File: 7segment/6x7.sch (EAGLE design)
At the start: 22 parts, among them IC1 AT90S2313P, IC2 7805TV

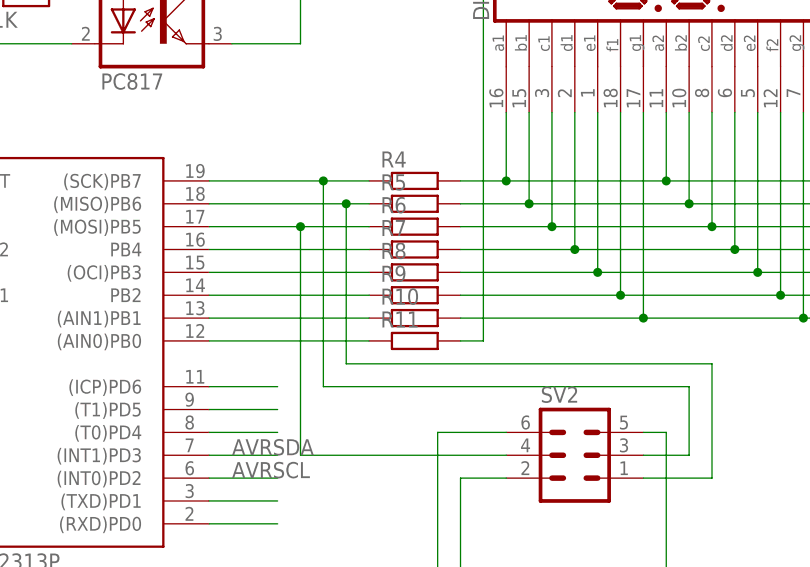
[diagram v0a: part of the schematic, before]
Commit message: 7segment 6x7: Add LED resistor values
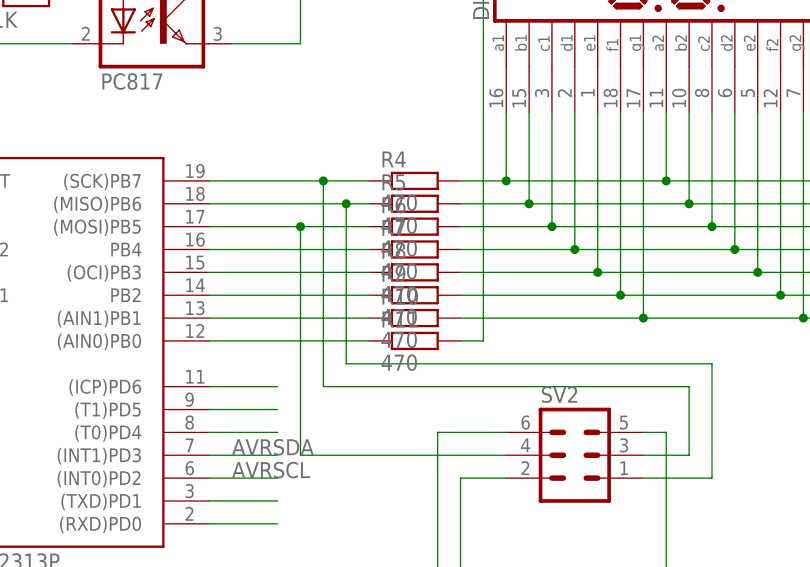
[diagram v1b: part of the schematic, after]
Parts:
- R10, R11, R4, R5, R6, R7, R8, R9: value (none) -> 470
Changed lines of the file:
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@@
 <part name="DIS2" library="display-hp" deviceset="HD-K121" device=""/>
 <part name="DIS3" library="display-hp" deviceset="HD-K121" device=""/>
-<part name="R4" library="rcl" deviceset="R-EU_" device="0207/10"/>
-<part name="R5" library="rcl" deviceset="R-EU_" device="0207/10"/>
-<part name="R6" library="rcl" deviceset="R-EU_" device="0207/10"/>
-<part name="R7" library="rcl" deviceset="R-EU_" device="0207/10"/>
-<part name="R8" library="rcl" deviceset="R-EU_" device="0207/10"/>
-<part name="R9" library="rcl" deviceset="R-EU_" device="0207/10"/>
-<part name="R10" library="rcl" deviceset="R-EU_" device="0207/10"/>
-<part name="R11" library="rcl" deviceset="R-EU_" device="0207/10"/>
+<part name="R4" library="rcl" deviceset="R-EU_" device="0207/10" value="470"/>
+<part name="R5" library="rcl" deviceset="R-EU_" device="0207/10" value="470"/>
+<part name="R6" library="rcl" deviceset="R-EU_" device="0207/10" value="470"/>
+<part name="R7" library="rcl" deviceset="R-EU_" device="0207/10" value="470"/>
+<part name="R8" library="rcl" deviceset="R-EU_" device="0207/10" value="470"/>
+<part name="R9" library="rcl" deviceset="R-EU_" device="0207/10" value="470"/>
+<part name="R10" library="rcl" deviceset="R-EU_" device="0207/10" value="470"/>
+<part name="R11" library="rcl" deviceset="R-EU_" device="0207/10" value="470"/>
 <part name="SV2" library="con-harting-ml" deviceset="ML6" device=""/>
 </parts>

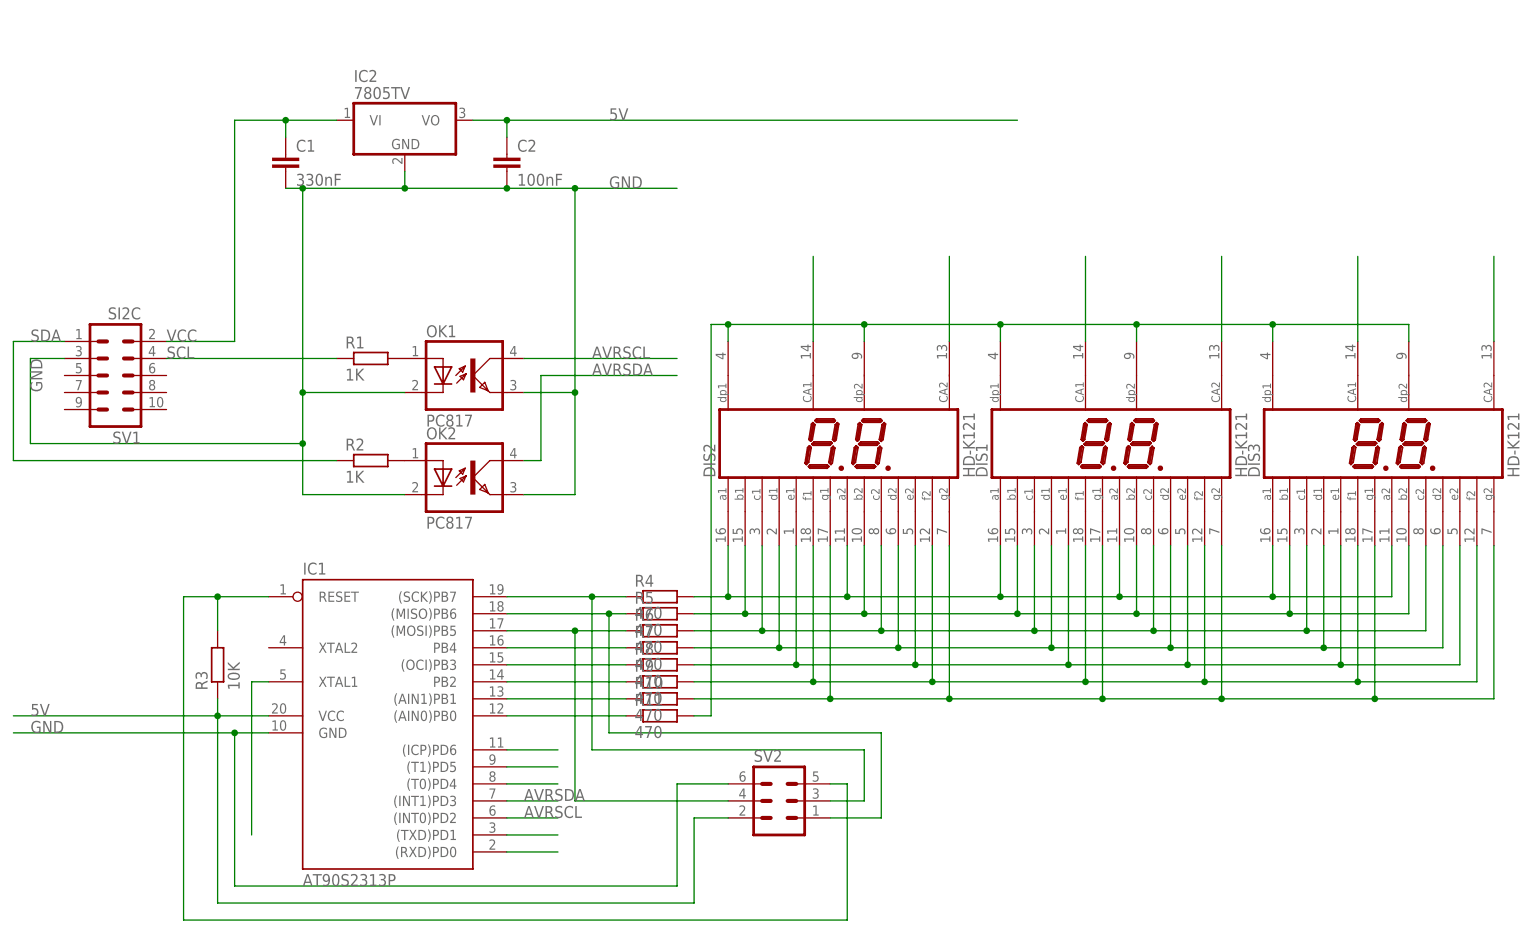
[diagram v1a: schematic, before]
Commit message: 7segment: schematic: add drill holes and netname labels
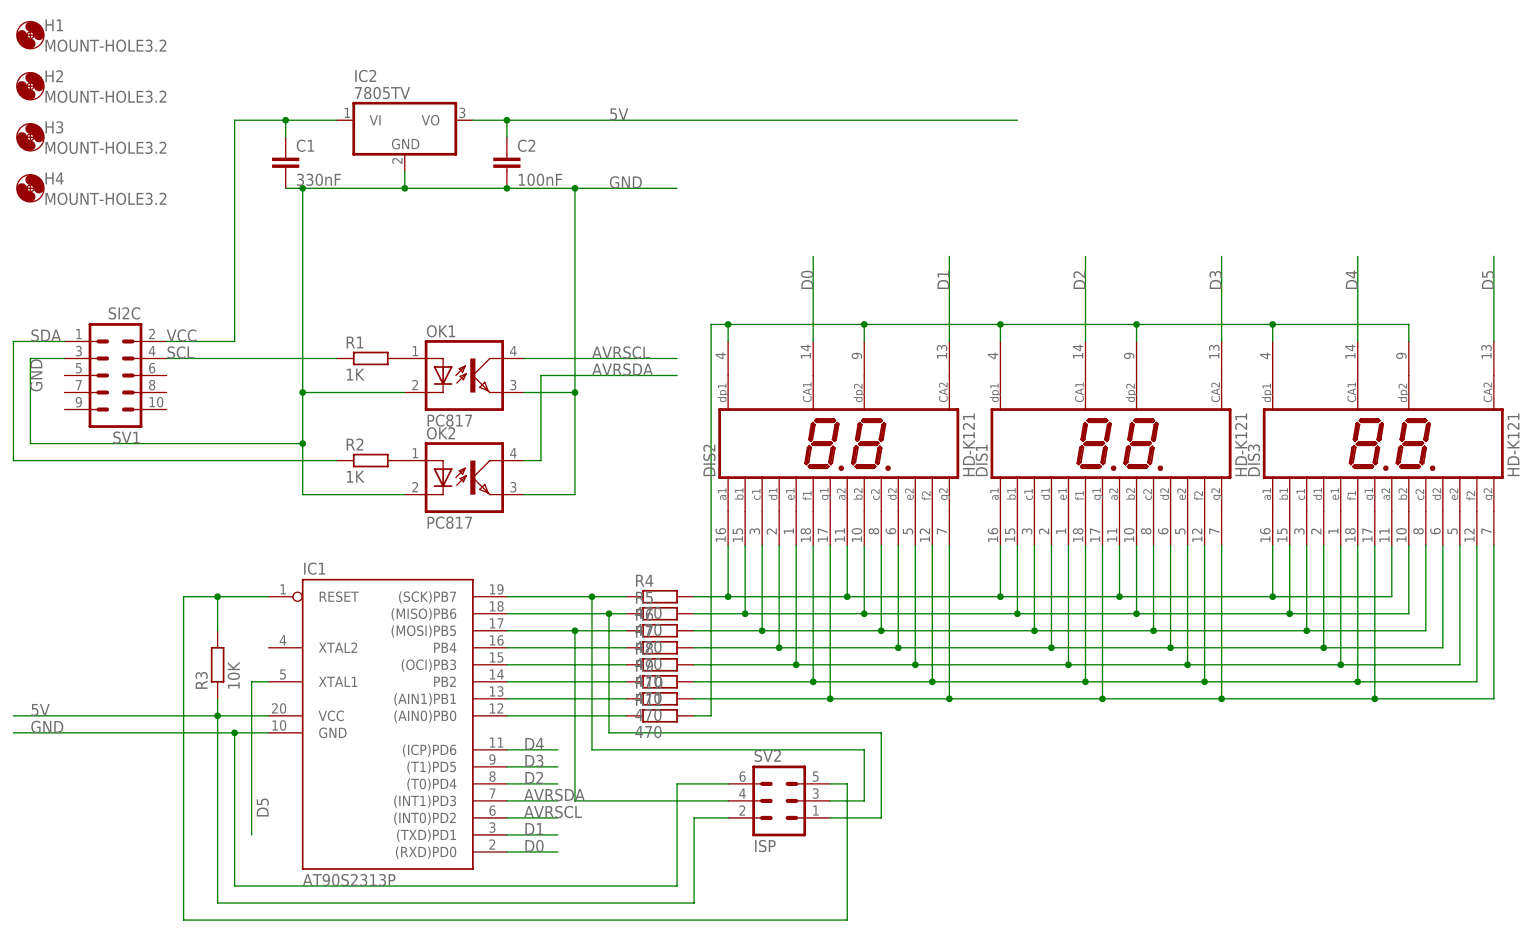
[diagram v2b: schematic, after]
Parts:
- added H1, H2, H3, H4: MOUNT-HOLE3.2, holes:MOUNT-HOLE3.2
- SV2: value (none) -> ISP
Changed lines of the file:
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@@
 <part name="R10" library="rcl" deviceset="R-EU_" device="0207/10" value="470"/>
 <part name="R11" library="rcl" deviceset="R-EU_" device="0207/10" value="470"/>
-<part name="SV2" library="con-harting-ml" deviceset="ML6" device=""/>
+<part name="SV2" library="con-harting-ml" deviceset="ML6" device="" value="ISP"/>
+<part name="H1" library="holes" deviceset="MOUNT-HOLE" device="3.2"/>
+<part name="H2" library="holes" deviceset="MOUNT-HOLE" device="3.2"/>
+<part name="H3" library="holes" deviceset="MOUNT-HOLE" device="3.2"/>
+<part name="H4" library="holes" deviceset="MOUNT-HOLE" device="3.2"/>
 </parts>
 <sheets>
@@
 <instance part="R11" gate="G$1" x="27.94" y="0"/>
 <instance part="SV2" gate="1" x="45.72" y="-12.7"/>
+<instance part="H1" gate="G$1" x="-66.04" y="101.6"/>
+<instance part="H2" gate="G$1" x="-66.04" y="93.98"/>
+<instance part="H3" gate="G$1" x="-66.04" y="86.36"/>
+<instance part="H4" gate="G$1" x="-66.04" y="78.74"/>
 </instances>
 <busses>
@@
 <pinref part="IC1" gate="G$1" pin="(RXD)PD0"/>
 <wire x1="5.08" y1="-20.32" x2="12.7" y2="-20.32" width="0.1524" layer="91"/>
+<label x="7.62" y="-20.32" size="1.778" layer="95"/>
 </segment>
 <segment>
 <pinref part="DIS2" gate="R" pin="CA1"/>
 <wire x1="50.8" y1="55.88" x2="50.8" y2="68.58" width="0.1524" layer="91"/>
+<label x="50.8" y="63.5" size="1.778" layer="95" rot="R90"/>
 </segment>
 </net>
@@
 <pinref part="IC1" gate="G$1" pin="(TXD)PD1"/>
 <wire x1="5.08" y1="-17.78" x2="12.7" y2="-17.78" width="0.1524" layer="91"/>
+<label x="7.62" y="-17.78" size="1.778" layer="95"/>
 </segment>
 <segment>
 <pinref part="DIS2" gate="R" pin="CA2"/>
 <wire x1="71.12" y1="55.88" x2="71.12" y2="68.58" width="0.1524" layer="91"/>
+<label x="71.12" y="63.5" size="1.778" layer="95" rot="R90"/>
 </segment>
 </net>
@@
 <pinref part="IC1" gate="G$1" pin="(T0)PD4"/>
 <wire x1="5.08" y1="-10.16" x2="12.7" y2="-10.16" width="0.1524" layer="91"/>
+<label x="7.62" y="-10.16" size="1.778" layer="95"/>
 </segment>
 <segment>
 <pinref part="DIS1" gate="R" pin="CA1"/>
 <wire x1="91.44" y1="55.88" x2="91.44" y2="68.58" width="0.1524" layer="91"/>
+<label x="91.44" y="63.5" size="1.778" layer="95" rot="R90"/>
 </segment>
 </net>
@@
 <pinref part="IC1" gate="G$1" pin="(T1)PD5"/>
 <wire x1="5.08" y1="-7.62" x2="12.7" y2="-7.62" width="0.1524" layer="91"/>
+<label x="7.62" y="-7.62" size="1.778" layer="95"/>
 </segment>
 <segment>
 <pinref part="DIS1" gate="R" pin="CA2"/>
 <wire x1="111.76" y1="55.88" x2="111.76" y2="68.58" width="0.1524" layer="91"/>
+<label x="111.76" y="63.5" size="1.778" layer="95" rot="R90"/>
 </segment>
 </net>
@@
 <pinref part="IC1" gate="G$1" pin="(ICP)PD6"/>
 <wire x1="5.08" y1="-5.08" x2="12.7" y2="-5.08" width="0.1524" layer="91"/>
+<label x="7.62" y="-5.08" size="1.778" layer="95"/>
 </segment>
 <segment>
 <pinref part="DIS3" gate="R" pin="CA1"/>
 <wire x1="132.08" y1="55.88" x2="132.08" y2="68.58" width="0.1524" layer="91"/>
+<label x="132.08" y="63.5" size="1.778" layer="95" rot="R90"/>
 </segment>
 </net>
@@
 <wire x1="-30.48" y1="5.08" x2="-33.02" y2="5.08" width="0.1524" layer="91"/>
 <wire x1="-33.02" y1="5.08" x2="-33.02" y2="-17.78" width="0.1524" layer="91"/>
+<label x="-30.48" y="-15.24" size="1.778" layer="95" rot="R90"/>
 </segment>
 <segment>
 <pinref part="DIS3" gate="R" pin="CA2"/>
 <wire x1="152.4" y1="55.88" x2="152.4" y2="68.58" width="0.1524" layer="91"/>
-</segment>
-</net>
+<label x="152.4" y="63.5" size="1.778" layer="95" rot="R90"/>
+</segment>
+</net>

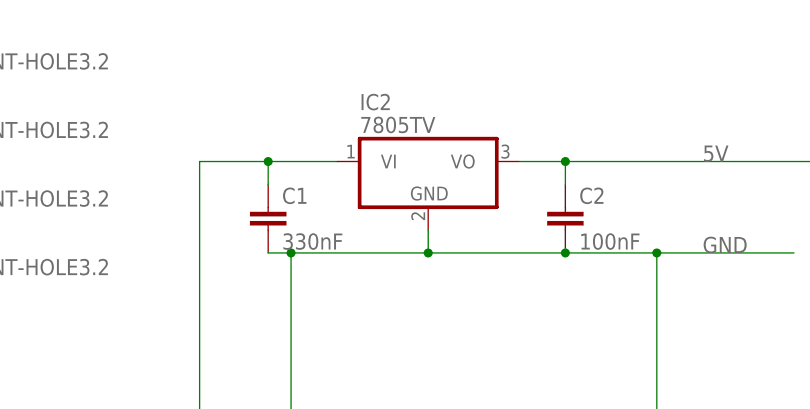
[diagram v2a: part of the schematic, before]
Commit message: 7segment: re-order parts for nicer(?) layout. TODO: routing
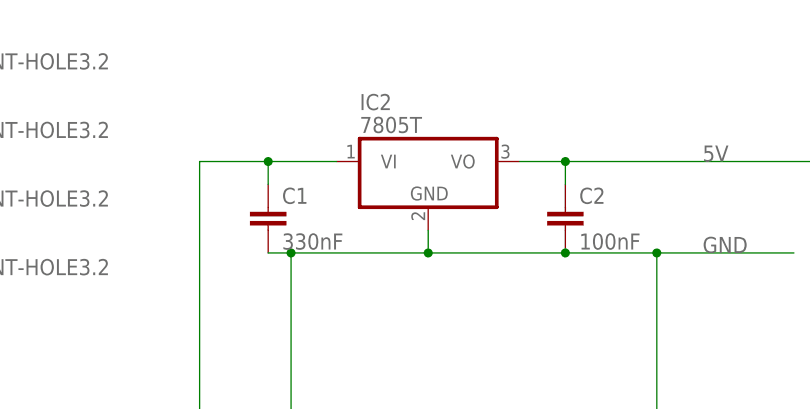
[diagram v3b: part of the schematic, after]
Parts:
- IC2: value 7805TV -> 7805T; device linear:7805TV -> linear:7805T
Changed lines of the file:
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@@
 <part name="OK1" library="optocoupler" deviceset="PC817" device=""/>
 <part name="OK2" library="optocoupler" deviceset="PC817" device=""/>
-<part name="IC2" library="linear" deviceset="78*" device="TV" technology="05"/>
+<part name="IC2" library="linear" deviceset="78*" device="T" technology="05" value="7805T"/>
 <part name="R1" library="rcl" deviceset="R-EU_" device="0207/10" value="1K"/>
 <part name="R2" library="rcl" deviceset="R-EU_" device="0207/10" value="1K"/>
